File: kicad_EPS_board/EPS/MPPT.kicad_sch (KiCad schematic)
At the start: 5 parts

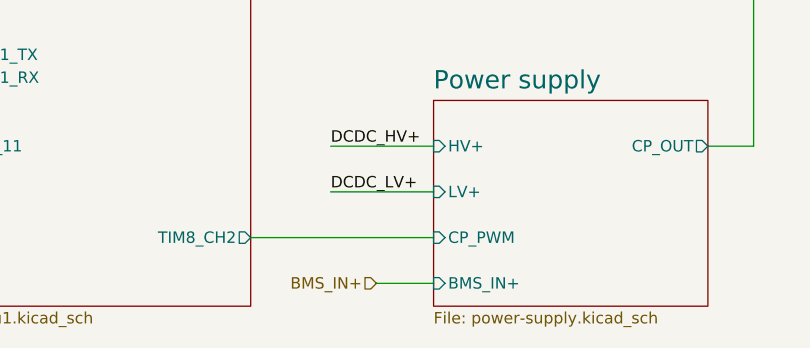
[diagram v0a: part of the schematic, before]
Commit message: kicad EPS board V2 revision and already generated html doc files
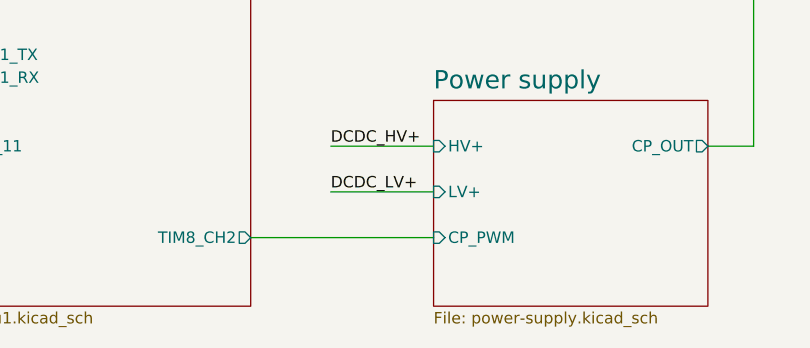
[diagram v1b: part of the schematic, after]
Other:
- sheet Power supply ports: added none; removed BMS_IN+
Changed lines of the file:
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@@
 (kicad_sch
-	(version 20231120)
+	(version 20250114)
 	(generator "eeschema")
-	(generator_version "8.0")
+	(generator_version "9.0")
 	(paper "A4")
+	(text "MPPT: 60V 10A"
+		(exclude_from_sim no)
+		(at 42.672 34.29 0)
+		(effects
+			(font
+				(size 2.032 2.032)
+			)
+			(justify right bottom)
+		)
+	)
+	(text "Load output: 20A"
+		(exclude_from_sim no)
+		(at 234.95 84.328 0)
+		(effects
+			(font
+				(size 2.032 2.032)
+			)
+			(justify left bottom)
+		)
+	)
+	(text "MPPT charge controller with HS load switch and CAN"
+		(exclude_from_sim no)
+		(at 43.18 26.67 0)
+		(effects
+			(font
+				(size 5.08 5.08)
+			)
+			(justify left bottom)
+		)
+	)
+	(text "Battery: 12V/24V 20A"
+		(exclude_from_sim no)
+		(at 224.79 41.656 0)
+		(effects
+			(font
+				(size 2.032 2.032)
+			)
+			(justify left bottom)
+		)
+	)
 	(junction
 		(at 215.9 57.15)
@@
 	(wire
 		(pts
-			(xy 176.53 153.67) (xy 182.88 153.67)
-		)
-		(stroke
-			(width 0)
-			(type default)
-		)
-	)
-	(wire
-		(pts
 			(xy 45.72 138.43) (xy 55.88 138.43)
 		)
@@
 			(width 0)
 			(type default)
-		)
-	)
-	(text "MPPT: 60V 10A"
-		(exclude_from_sim no)
-		(at 42.672 34.29 0)
-		(effects
-			(font
-				(size 2.032 2.032)
-			)
-			(justify right bottom)
-		)
-	)
-	(text "Load output: 20A"
-		(exclude_from_sim no)
-		(at 234.95 84.328 0)
-		(effects
-			(font
-				(size 2.032 2.032)
-			)
-			(justify left bottom)
-		)
-	)
-	(text "MPPT charge controller with HS load switch and CAN"
-		(exclude_from_sim no)
-		(at 43.18 26.67 0)
-		(effects
-			(font
-				(size 5.08 5.08)
-			)
-			(justify left bottom)
-		)
-	)
-	(text "Battery: 12V/24V 20A"
-		(exclude_from_sim no)
-		(at 224.79 41.656 0)
-		(effects
-			(font
-				(size 2.032 2.032)
-			)
-			(justify left bottom)
 		)
 	)
@@
 		(shape input)
 		(at 33.02 52.07 180)
-		(effects
-			(font
-				(size 1.27 1.27)
-			)
-			(justify right)
-		)
-	)
-	(hierarchical_label "BMS_IN+"
-		(shape input)
-		(at 176.53 153.67 180)
 		(effects
 			(font
@@
 		(at 76.2 41.91)
 		(size 30.48 43.18)
+		(exclude_from_sim no)
+		(in_bom yes)
+		(on_board yes)
+		(dnp no)
 		(fields_autoplaced yes)
 		(stroke
@@
 		(at 182.88 133.35)
 		(size 30.48 22.86)
+		(exclude_from_sim no)
+		(in_bom yes)
+		(on_board yes)
+		(dnp no)
 		(fields_autoplaced yes)
 		(stroke
@@
 				)
 				(justify right)
-			)
-		)
-		(pin "BMS_IN+" input
-			(at 182.88 153.67 180)
-			(effects
-				(font
-					(size 1.27 1.27)
-				)
-				(justify left)
 			)
 		)
@@
 		(at 76.2 120.65)
 		(size 30.48 27.94)
+		(exclude_from_sim no)
+		(in_bom yes)
+		(on_board yes)
+		(dnp no)
 		(fields_autoplaced yes)
 		(stroke
@@
 		(at 182.88 77.47)
 		(size 30.48 40.64)
+		(exclude_from_sim no)
+		(in_bom yes)
+		(on_board yes)
+		(dnp no)
 		(fields_autoplaced yes)
 		(stroke
@@
 		(at 127 57.15)
 		(size 35.56 99.06)
+		(exclude_from_sim no)
+		(in_bom yes)
+		(on_board yes)
+		(dnp no)
 		(fields_autoplaced yes)
 		(stroke
